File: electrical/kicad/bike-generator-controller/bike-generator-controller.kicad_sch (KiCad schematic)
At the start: 0 parts

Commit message: feat(pcb): finalize V1 controller layout
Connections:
- no-connect marks 1 -> 2
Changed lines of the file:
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@@
 		(at 88.9 132.08)
+	)
+	(no_connect
+		(at 176.53 134.62)
 	)
 	(wire

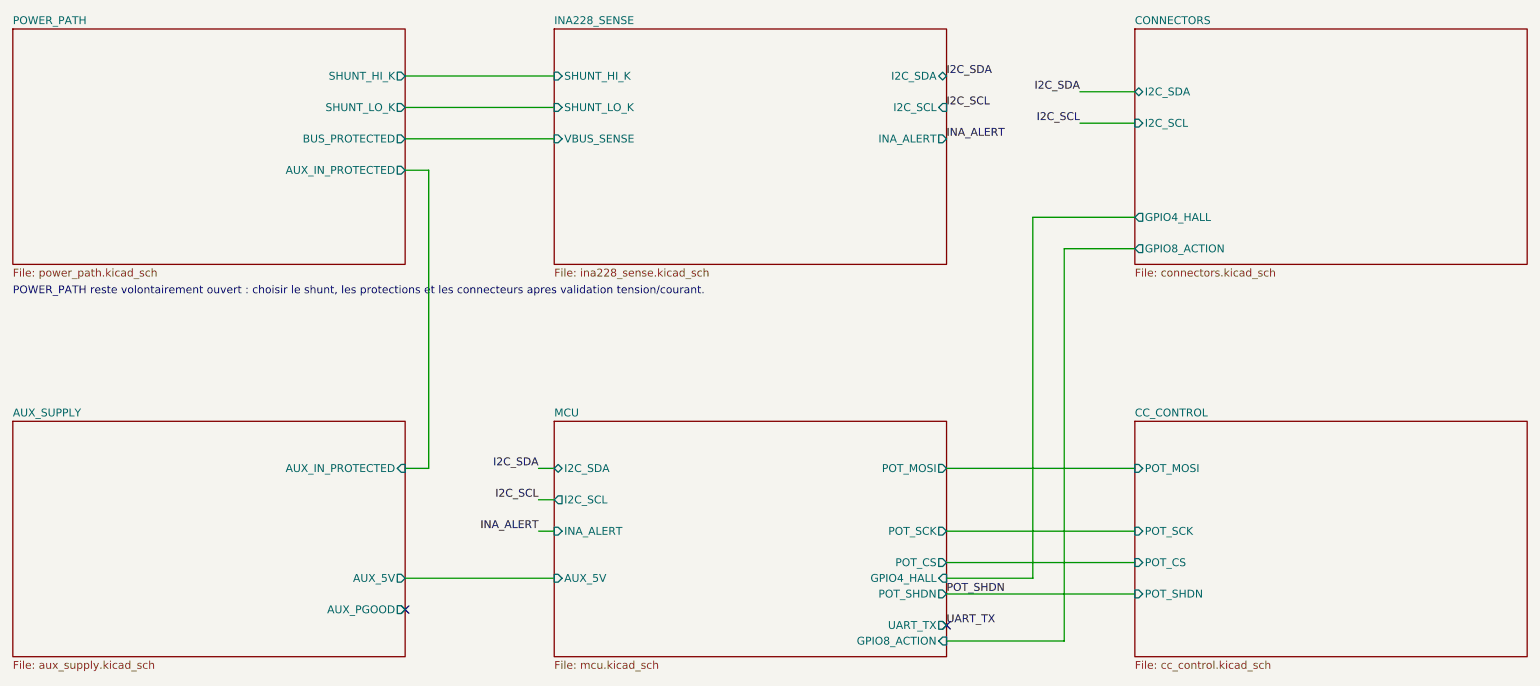
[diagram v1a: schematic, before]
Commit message: feat(controller): finalize V1 design and sourcing
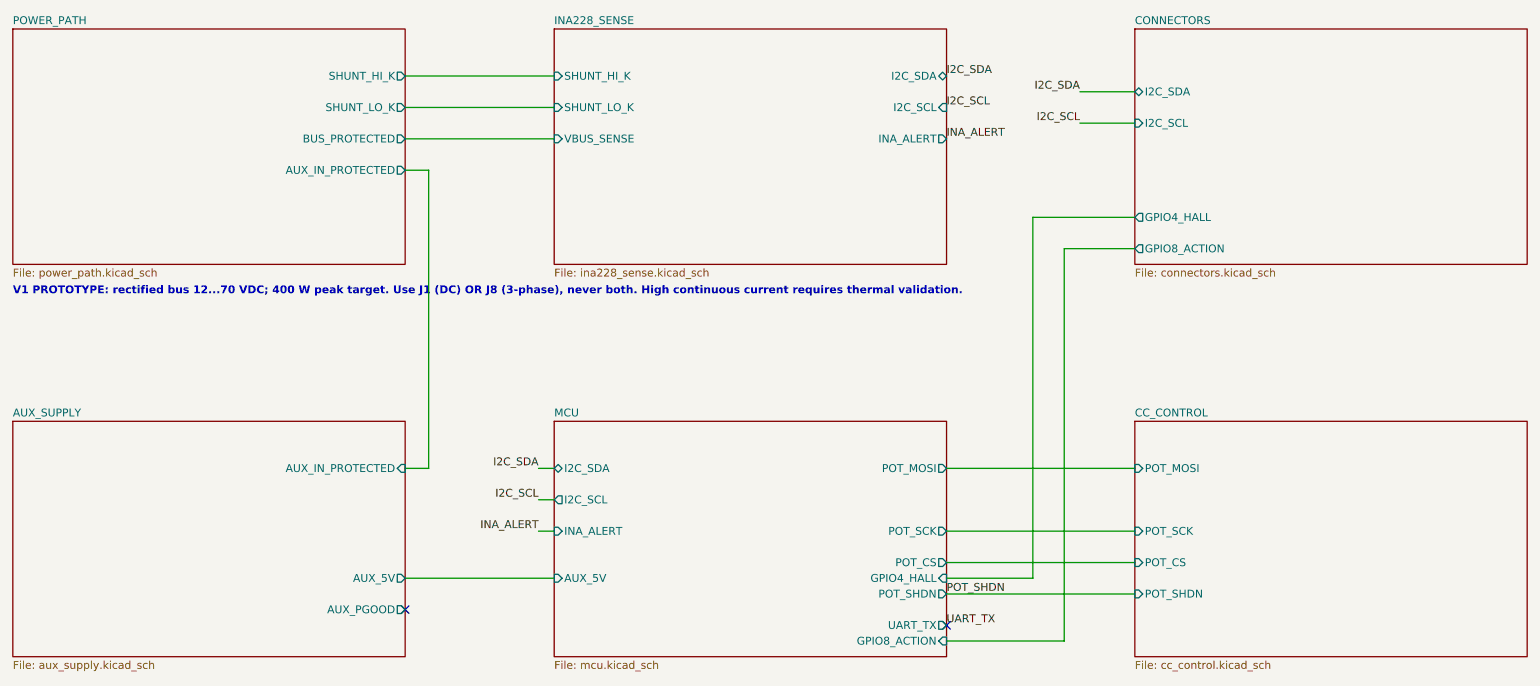
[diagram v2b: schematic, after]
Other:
- note added: "V1 PROTOTYPE: rectified bus 12...70 VDC; 400 W peak target. Use J1 (DC) OR J8 (3-phase), never both. High continuous current requires thermal validation."
- note removed: "POWER_PATH reste volontairement ouvert : choisir le shunt, les protections et les connecteurs apres validation tension/courant."
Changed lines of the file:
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@@
 	(generator_version "10.0")
 	(paper "A4")
-	(text "POWER_PATH reste volontairement ouvert : choisir le shunt, les protections et les connecteurs apres validation tension/courant."
+	(text "V1 PROTOTYPE: rectified bus 12...70 VDC; 400 W peak target. Use J1 (DC) OR J8 (3-phase), never both. High continuous current requires thermal validation."
 		(exclude_from_sim no)
 		(at 25.4 81.28 0)
@@
 			(font
 				(size 1.27 1.27)
+				(bold yes)
 			)
 			(justify left bottom)
